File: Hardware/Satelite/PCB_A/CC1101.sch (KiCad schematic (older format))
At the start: 18 parts, among them U2 CC1101RGP, U3 0915BM15A0001E, Y1 26 MHz

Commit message: PCB_A mas cambios
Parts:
- C10, C11, C12, C4, C5, C6, C7, C8, C9: footprint Capacitor_SMD:C_0603_1608Metric -> Capacitor_SMD:C_0402_1005Metric
- R8: footprint Resistor_SMD:R_0603_1608Metric_Pad1.05x0.95mm_HandSolder -> Resistor_SMD:R_0402_1005Metric
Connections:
- net GND: no longer U2.7 (CSN)
- new net CS: U2.7 (CSN)
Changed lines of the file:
@@
 Text HLabel 2800 2200 0    50   Input ~ 0
 SI
-$Comp
-L power:GND #PWR?
-U 1 1 5BCB61A6
-P 3400 4600
-AR Path="/5B9A8077/5BCB61A6" Ref="#PWR?"  Part="1"
-AR Path="/5BA17F9C/5BCB61A6" Ref="#PWR027"  Part="1"
-F 0 "#PWR027" H 3400 4350 50  0001 C CNN
-F 1 "GND" H 3405 4427 50  0000 C CNN
-F 2 "" H 3400 4600 50  0001 C CNN
-F 3 "" H 3400 4600 50  0001 C CNN
-	1    3400 4600
-	1    0    0    -1
-$EndComp
 Wire Wire Line
 	3400 4600 3400 4450
@@
 P 2150 4000
 AR Path="/5B9A8077/5BCB61D1" Ref="#PWR?"  Part="1"
-AR Path="/5BA17F9C/5BCB61D1" Ref="#PWR024"  Part="1"
-F 0 "#PWR024" H 2150 3750 50  0001 C CNN
+AR Path="/5BA17F9C/5BCB61D1" Ref="#PWR025"  Part="1"
+F 0 "#PWR025" H 2150 3750 50  0001 C CNN
 F 1 "GND" H 2155 3827 50  0000 C CNN
 F 2 "" H 2150 4000 50  0001 C CNN
@@
 P 2550 4000
 AR Path="/5B9A8077/5BCB61D7" Ref="#PWR?"  Part="1"
-AR Path="/5BA17F9C/5BCB61D7" Ref="#PWR025"  Part="1"
-F 0 "#PWR025" H 2550 3750 50  0001 C CNN
+AR Path="/5BA17F9C/5BCB61D7" Ref="#PWR026"  Part="1"
+F 0 "#PWR026" H 2550 3750 50  0001 C CNN
 F 1 "GND" H 2555 3827 50  0000 C CNN
 F 2 "" H 2550 4000 50  0001 C CNN
@@
 F 0 "R8" H 3770 2096 50  0000 L CNN
 F 1 "56k" H 3770 2005 50  0000 L CNN
-F 2 "Resistor_SMD:R_0603_1608Metric_Pad1.05x0.95mm_HandSolder" V 3630 2050 50  0001 C CNN
+F 2 "Resistor_SMD:R_0402_1005Metric" V 3630 2050 50  0001 C CNN
 F 3 "~" H 3700 2050 50  0001 C CNN
 	1    3700 2050
@@
 F 0 "C6" H 3392 2046 50  0000 L CNN
 F 1 "100nF" H 3392 1955 50  0000 L CNN
-F 2 "Capacitor_SMD:C_0603_1608Metric" H 3300 2000 50  0001 C CNN
+F 2 "Capacitor_SMD:C_0402_1005Metric" H 3300 2000 50  0001 C CNN
 F 3 "~" H 3300 2000 50  0001 C CNN
 F 4 "X7R" H 3300 2000 50  0001 C CNN "Dielectric"
@@
 F 0 "C4" H 2242 3696 50  0000 L CNN
 F 1 "100nF" H 2242 3605 50  0000 L CNN
-F 2 "Capacitor_SMD:C_0603_1608Metric" H 2150 3650 50  0001 C CNN
+F 2 "Capacitor_SMD:C_0402_1005Metric" H 2150 3650 50  0001 C CNN
 F 3 "~" H 2150 3650 50  0001 C CNN
 F 4 "X7R" H 2150 3650 50  0001 C CNN "Dielectric"
@@
 F 0 "C5" H 2642 3696 50  0000 L CNN
 F 1 "100nF" H 2642 3605 50  0000 L CNN
-F 2 "Capacitor_SMD:C_0603_1608Metric" H 2550 3650 50  0001 C CNN
+F 2 "Capacitor_SMD:C_0402_1005Metric" H 2550 3650 50  0001 C CNN
 F 3 "~" H 2550 3650 50  0001 C CNN
 F 4 "X7R" H 2550 3650 50  0001 C CNN "Dielectric"
@@
 F 0 "C10" H 4692 4846 50  0000 L CNN
 F 1 "100nF" H 4692 4755 50  0000 L CNN
-F 2 "Capacitor_SMD:C_0603_1608Metric" H 4600 4800 50  0001 C CNN
+F 2 "Capacitor_SMD:C_0402_1005Metric" H 4600 4800 50  0001 C CNN
 F 3 "~" H 4600 4800 50  0001 C CNN
 F 4 "X7R" H 4600 4800 50  0001 C CNN "Dielectric"
@@
 F 0 "C9" H 4492 3696 50  0000 L CNN
 F 1 "100nF" H 4492 3605 50  0000 L CNN
-F 2 "Capacitor_SMD:C_0603_1608Metric" H 4400 3650 50  0001 C CNN
+F 2 "Capacitor_SMD:C_0402_1005Metric" H 4400 3650 50  0001 C CNN
 F 3 "~" H 4400 3650 50  0001 C CNN
 F 4 "X7R" H 4400 3650 50  0001 C CNN "Dielectric"
@@
 F 0 "C11" H 4892 3296 50  0000 L CNN
 F 1 "100nF" H 4892 3205 50  0000 L CNN
-F 2 "Capacitor_SMD:C_0603_1608Metric" H 4800 3250 50  0001 C CNN
+F 2 "Capacitor_SMD:C_0402_1005Metric" H 4800 3250 50  0001 C CNN
 F 3 "~" H 4800 3250 50  0001 C CNN
 F 4 "X7R" H 4800 3250 50  0001 C CNN "Dielectric"
@@
 F 0 "C12" H 5292 3296 50  0000 L CNN
 F 1 "100nF" H 5292 3205 50  0000 L CNN
-F 2 "Capacitor_SMD:C_0603_1608Metric" H 5200 3250 50  0001 C CNN
+F 2 "Capacitor_SMD:C_0402_1005Metric" H 5200 3250 50  0001 C CNN
 F 3 "~" H 5200 3250 50  0001 C CNN
 F 4 "X7R" H 5200 3250 50  0001 C CNN "Dielectric"
@@
 F 0 "C7" H 3592 5296 50  0000 L CNN
 F 1 "18pF" H 3592 5205 50  0000 L CNN
-F 2 "Capacitor_SMD:C_0603_1608Metric" H 3500 5250 50  0001 C CNN
+F 2 "Capacitor_SMD:C_0402_1005Metric" H 3500 5250 50  0001 C CNN
 F 3 "~" H 3500 5250 50  0001 C CNN
 F 4 "NP0" H 3500 5250 50  0001 C CNN "Dielectric"
@@
 F 0 "C8" H 3992 5296 50  0000 L CNN
 F 1 "18pF" H 3992 5205 50  0000 L CNN
-F 2 "Capacitor_SMD:C_0603_1608Metric" H 3900 5250 50  0001 C CNN
+F 2 "Capacitor_SMD:C_0402_1005Metric" H 3900 5250 50  0001 C CNN
 F 3 "~" H 3900 5250 50  0001 C CNN
 F 4 "NP0" H 3900 5250 50  0001 C CNN "Dielectric"
@@
 P 2800 2600
 AR Path="/5B9A8077/5BCB6317" Ref="#PWR?"  Part="1"
-AR Path="/5BA17F9C/5BCB6317" Ref="#PWR026"  Part="1"
-F 0 "#PWR026" H 2800 2350 50  0001 C CNN
+AR Path="/5BA17F9C/5BCB6317" Ref="#PWR027"  Part="1"
+F 0 "#PWR027" H 2800 2350 50  0001 C CNN
 F 1 "GND" H 2805 2427 50  0000 C CNN
 F 2 "" H 2800 2600 50  0001 C CNN
@@
 P 2150 3300
 AR Path="/5BCBBE88" Ref="#PWR?"  Part="1"
-AR Path="/5BA17F9C/5BCBBE88" Ref="#PWR23"  Part="1"
-F 0 "#PWR23" H 2150 3700 50  0001 C CNN
+AR Path="/5BA17F9C/5BCBBE88" Ref="#PWR24"  Part="1"
+F 0 "#PWR24" H 2150 3700 50  0001 C CNN
 F 1 "+3V3_Internal" H 2135 3473 50  0000 C CNN
 F 2 "" H 2150 3300 50  0001 C CNN
@@
 	1    0    0    -1
 $EndComp
+Text HLabel 3300 4600 0    50   Output ~ 0
+CS
+Wire Wire Line
+	3300 4600 3400 4600
 $EndSCHEMATC

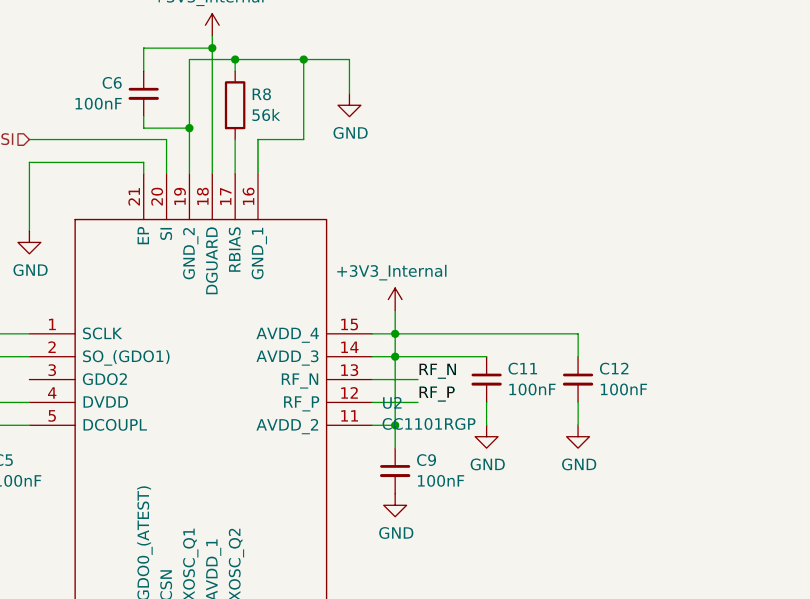
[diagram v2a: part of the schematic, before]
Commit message: Capacitores 0402 para PCB_C
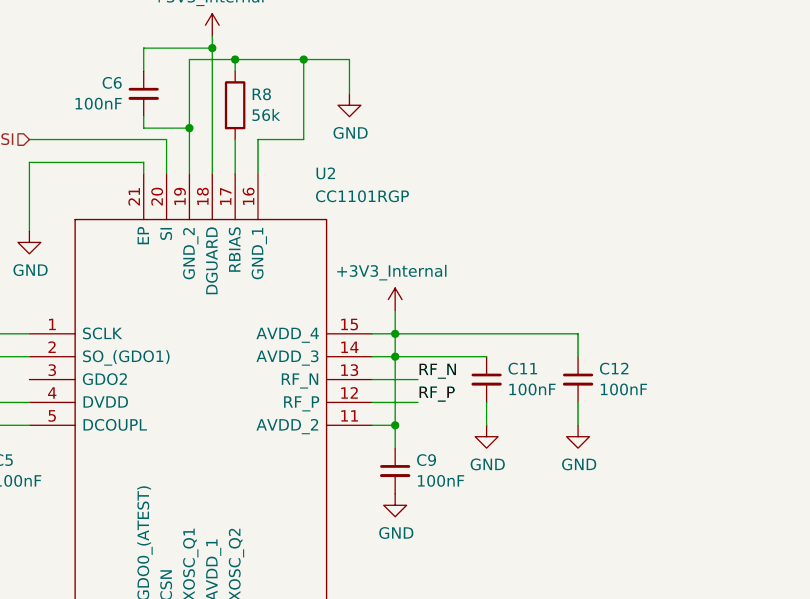
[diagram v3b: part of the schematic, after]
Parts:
- C10, C11, C12, C4, C5, C6, C9: Manufacturer Part Number EMK107B7104KAHT -> GCM155R71C104KA55D
- C7, C8: Manufacturer Part Number VJ0603A180KXQPW1BC -> C0402C180J5GACTU
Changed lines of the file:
@@
 F 4 "X7R" H 3300 2000 50  0001 C CNN "Dielectric"
 F 5 "16V" H 3300 2000 50  0001 C CNN "Voltage"
-F 6 "EMK107B7104KAHT" H 3300 2000 50  0001 C CNN "Manufacturer Part Number"
+F 6 "GCM155R71C104KA55D" H 3300 2000 50  0001 C CNN "Manufacturer Part Number"
 	1    3300 2000
 	-1   0    0    -1
@@
 F 4 "X7R" H 2150 3650 50  0001 C CNN "Dielectric"
 F 5 "16V" H 2150 3650 50  0001 C CNN "Voltage"
-F 6 "EMK107B7104KAHT" H 2150 3650 50  0001 C CNN "Manufacturer Part Number"
+F 6 "GCM155R71C104KA55D" H 2150 3650 50  0001 C CNN "Manufacturer Part Number"
 	1    2150 3650
 	1    0    0    -1
@@
 F 4 "X7R" H 2550 3650 50  0001 C CNN "Dielectric"
 F 5 "16V" H 2550 3650 50  0001 C CNN "Voltage"
-F 6 "EMK107B7104KAHT" H 2550 3650 50  0001 C CNN "Manufacturer Part Number"
+F 6 "GCM155R71C104KA55D" H 2550 3650 50  0001 C CNN "Manufacturer Part Number"
 	1    2550 3650
 	1    0    0    -1
@@
 F 4 "X7R" H 4600 4800 50  0001 C CNN "Dielectric"
 F 5 "16V" H 4600 4800 50  0001 C CNN "Voltage"
-F 6 "EMK107B7104KAHT" H 4600 4800 50  0001 C CNN "Manufacturer Part Number"
+F 6 "GCM155R71C104KA55D" H 4600 4800 50  0001 C CNN "Manufacturer Part Number"
 	1    4600 4800
 	1    0    0    -1
@@
 F 4 "X7R" H 4400 3650 50  0001 C CNN "Dielectric"
 F 5 "16V" H 4400 3650 50  0001 C CNN "Voltage"
-F 6 "EMK107B7104KAHT" H 4400 3650 50  0001 C CNN "Manufacturer Part Number"
+F 6 "GCM155R71C104KA55D" H 4400 3650 50  0001 C CNN "Manufacturer Part Number"
 	1    4400 3650
 	1    0    0    -1
@@
 F 4 "X7R" H 4800 3250 50  0001 C CNN "Dielectric"
 F 5 "16V" H 4800 3250 50  0001 C CNN "Voltage"
-F 6 "EMK107B7104KAHT" H 4800 3250 50  0001 C CNN "Manufacturer Part Number"
+F 6 "GCM155R71C104KA55D" H 4800 3250 50  0001 C CNN "Manufacturer Part Number"
 	1    4800 3250
 	1    0    0    -1
@@
 F 4 "X7R" H 5200 3250 50  0001 C CNN "Dielectric"
 F 5 "16V" H 5200 3250 50  0001 C CNN "Voltage"
-F 6 "EMK107B7104KAHT" H 5200 3250 50  0001 C CNN "Manufacturer Part Number"
+F 6 "GCM155R71C104KA55D" H 5200 3250 50  0001 C CNN "Manufacturer Part Number"
 	1    5200 3250
 	1    0    0    -1
@@
 F 4 "NP0" H 3500 5250 50  0001 C CNN "Dielectric"
 F 5 "10V" H 3500 5250 50  0001 C CNN "Voltage"
-F 6 "VJ0603A180KXQPW1BC" H 3500 5250 50  0001 C CNN "Manufacturer Part Number"
+F 6 "C0402C180J5GACTU" H 3500 5250 50  0001 C CNN "Manufacturer Part Number"
 	1    3500 5250
 	-1   0    0    -1
@@
 F 4 "NP0" H 3900 5250 50  0001 C CNN "Dielectric"
 F 5 "10V" H 3900 5250 50  0001 C CNN "Voltage"
-F 6 "VJ0603A180KXQPW1BC" H 3900 5250 50  0001 C CNN "Manufacturer Part Number"
+F 6 "C0402C180J5GACTU" H 3900 5250 50  0001 C CNN "Manufacturer Part Number"
 	1    3900 5250
 	1    0    0    -1
@@
 AR Path="/5B9A8077/5BCB632A" Ref="U?"  Part="1"
 AR Path="/5BA17F9C/5BCB632A" Ref="U2"  Part="1"
-F 0 "U2" H 4341 2746 50  0000 L CNN
-F 1 "CC1101RGP" H 4341 2654 50  0000 L CNN
+F 0 "U2" H 4050 3750 50  0000 L CNN
+F 1 "CC1101RGP" H 4050 3650 50  0000 L CNN
 F 2 "SamacSys_Parts:QFN50P400X400X100-21N-D" H 4150 3550 50  0001 L CNN
 F 3 "http://www.ti.com/lit/ds/symlink/cc1101.pdf" H 4150 3450 50  0001 L CNN

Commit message: Numeros de parte para PCB_A. Se movió también el switch de encendido más afuera para fácil acceso.
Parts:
- R8: Manufacturer Part Number (none) -> RC0402FR-0756KL
- U2: Manufacturer Part Number (none) -> CC1101RGP; Manufacturer_Part_Number CC1101RGP -> (none)
- U3: Manufacturer Part Number (none) -> 0915BM15A0001E; Manufacturer_Part_Number 0915BM15A0001E -> (none)
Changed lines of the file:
@@
 F 2 "Resistor_SMD:R_0402_1005Metric" V 3630 2050 50  0001 C CNN
 F 3 "~" H 3700 2050 50  0001 C CNN
+F 4 "RC0402FR-0756KL" H 3700 2050 50  0001 C CNN "Manufacturer Part Number"
 	1    3700 2050
 	1    0    0    -1
@@
 F 5 "0.8" H 7400 3200 50  0001 L CNN "Height"
 F 6 "JOHANSON TECHNOLOGY" H 7400 3100 50  0001 L CNN "Manufacturer_Name"
-F 7 "0915BM15A0001E" H 7400 3000 50  0001 L CNN "Manufacturer_Part_Number"
+F 7 "0915BM15A0001E" H 7400 3000 50  0001 L CNN "Manufacturer Part Number"
 F 8 "0915BM15A0001E" H 7400 2900 50  0001 L CNN "Arrow Part Number"
 	1    7050 3300
@@
 F 5 "1" H 4150 3250 50  0001 L CNN "Height"
 F 6 "Texas Instruments" H 4150 3150 50  0001 L CNN "Manufacturer_Name"
-F 7 "CC1101RGP" H 4150 3050 50  0001 L CNN "Manufacturer_Part_Number"
+F 7 "CC1101RGP" H 4150 3050 50  0001 L CNN "Manufacturer Part Number"
 F 8 "8203068P" H 4150 2950 50  0001 L CNN "RS Part Number"
 F 9 "http://uk.rs-online.com/web/p/products/8203068P" H 4150 2850 50  0001 L CNN "RS Price/Stock"

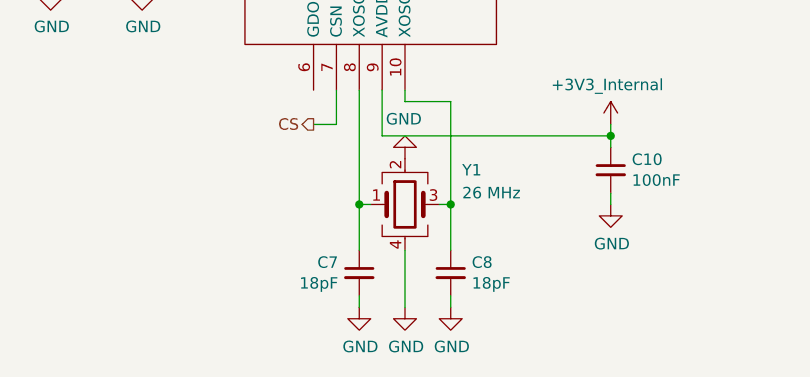
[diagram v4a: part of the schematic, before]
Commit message: Numeros de parte para estación terrena. Capacitores de 15pF para cristal de CC1101 (en lugar de 18pF).
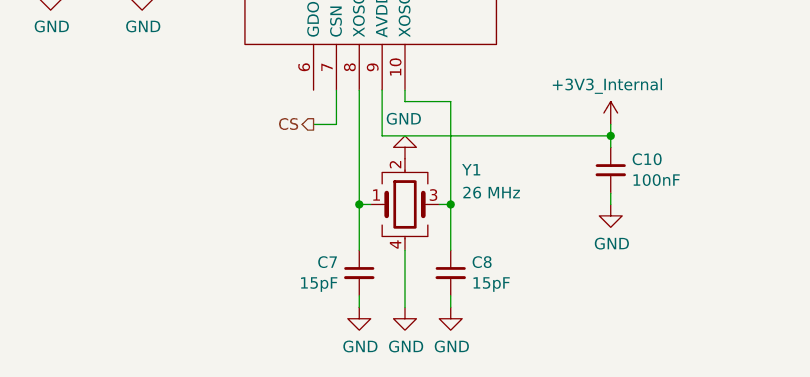
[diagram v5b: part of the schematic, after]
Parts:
- C7, C8: value 18pF -> 15pF; Manufacturer Part Number C0402C180J5GACTU -> C0402C150J5GACTU
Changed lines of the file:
@@
 AR Path="/5BA17F9C/5BCB62F1" Ref="C7"  Part="1"
 F 0 "C7" H 3592 5296 50  0000 L CNN
-F 1 "18pF" H 3592 5205 50  0000 L CNN
+F 1 "15pF" H 3592 5205 50  0000 L CNN
 F 2 "Capacitor_SMD:C_0402_1005Metric" H 3500 5250 50  0001 C CNN
 F 3 "~" H 3500 5250 50  0001 C CNN
 F 4 "NP0" H 3500 5250 50  0001 C CNN "Dielectric"
 F 5 "10V" H 3500 5250 50  0001 C CNN "Voltage"
-F 6 "C0402C180J5GACTU" H 3500 5250 50  0001 C CNN "Manufacturer Part Number"
+F 6 "C0402C150J5GACTU" H 3500 5250 50  0001 C CNN "Manufacturer Part Number"
 	1    3500 5250
 	-1   0    0    -1
@@
 AR Path="/5BA17F9C/5BCB62FB" Ref="C8"  Part="1"
 F 0 "C8" H 3992 5296 50  0000 L CNN
-F 1 "18pF" H 3992 5205 50  0000 L CNN
+F 1 "15pF" H 3992 5205 50  0000 L CNN
 F 2 "Capacitor_SMD:C_0402_1005Metric" H 3900 5250 50  0001 C CNN
 F 3 "~" H 3900 5250 50  0001 C CNN
 F 4 "NP0" H 3900 5250 50  0001 C CNN "Dielectric"
 F 5 "10V" H 3900 5250 50  0001 C CNN "Voltage"
-F 6 "C0402C180J5GACTU" H 3900 5250 50  0001 C CNN "Manufacturer Part Number"
+F 6 "C0402C150J5GACTU" H 3900 5250 50  0001 C CNN "Manufacturer Part Number"
 	1    3900 5250
 	1    0    0    -1
